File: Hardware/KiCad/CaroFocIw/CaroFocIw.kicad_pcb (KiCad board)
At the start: 4 copper layers, 174.5 x 99 mm, 130 parts, among them J1 Conn_01x04, J10 Conn_01x03, J11 Conn_01x03, J12 Conn_01x03, J13 Conn_01x03, J14 Conn_01x03, J15 Conn_01x06, J16 Conn_01x06, J17 Conn_01x06, J18 Conn_01x06, J19 Conn_01x02, J2 Conn_01x01, J20 Conn_01x02, J21 Conn_01x03, J22 Conn_01x03, J23 Conn_01x03, J24 Conn_01x03, J25 Conn_01x03, J26 Conn_01x03, J27 Conn_01x01, J28 Conn_01x01, J29 Conn_01x01, J3 Conn_01x01, J30 Conn_01x01, J4 Conn_01x01, J5 Conn_01x02, J6 Conn_01x01, J7 Conn_01x02, J8 Conn_01x02, J9 Conn_01x03, Q1 Q_NMOS_SGD, Q2 Q_NMOS_SGD, Q3 Q_NMOS_SGD, Q4 Q_NMOS_SGD, Q5 Q_NMOS_SGD, Q6 Q_NMOS_SGD, U1 TCAN332, U2 STM32F405RGTx, U3 TLE7185-1E, U4 ACS711xEXLT-15AB, U5 AS5048A, U6 ACS711xEXLT-15AB, U7 ACS711xEXLT-15AB, U8 LMR16006YQ3

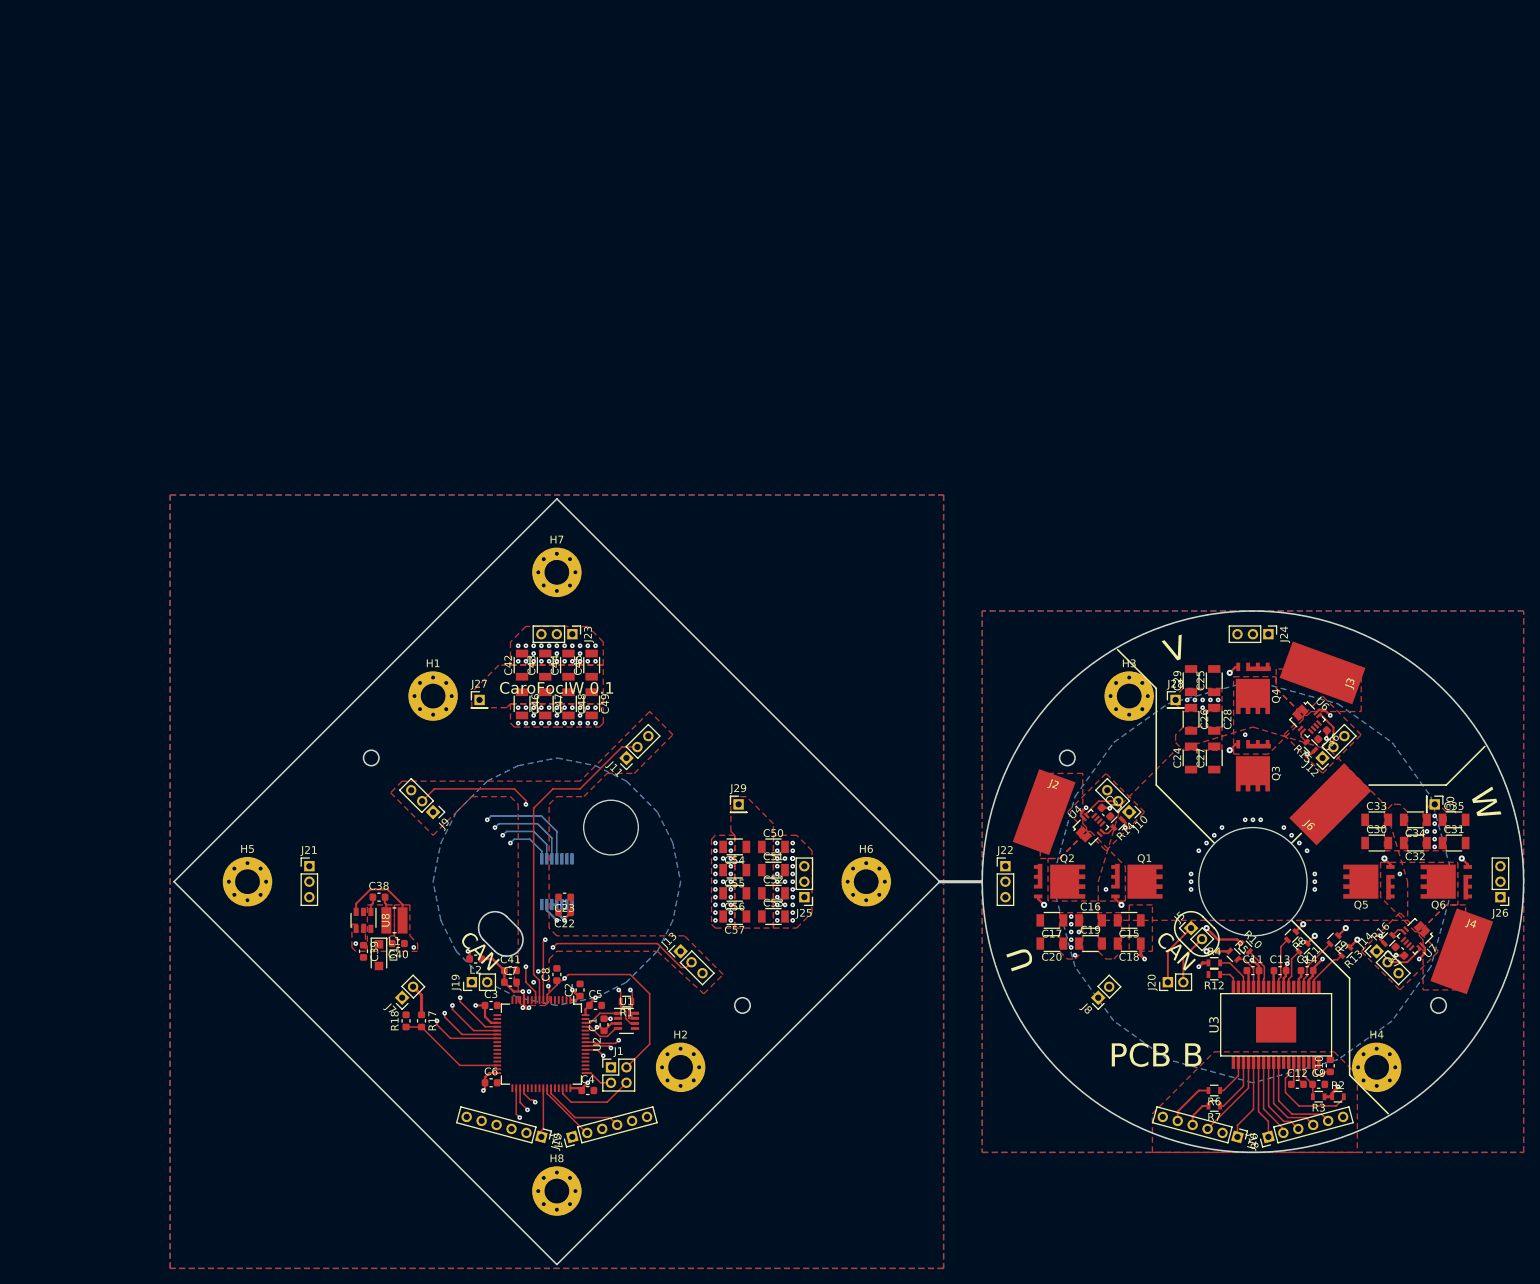
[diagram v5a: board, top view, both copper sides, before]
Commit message: Smaller form factor -> lots of rerouting needed. Moved gate driver to PCB A
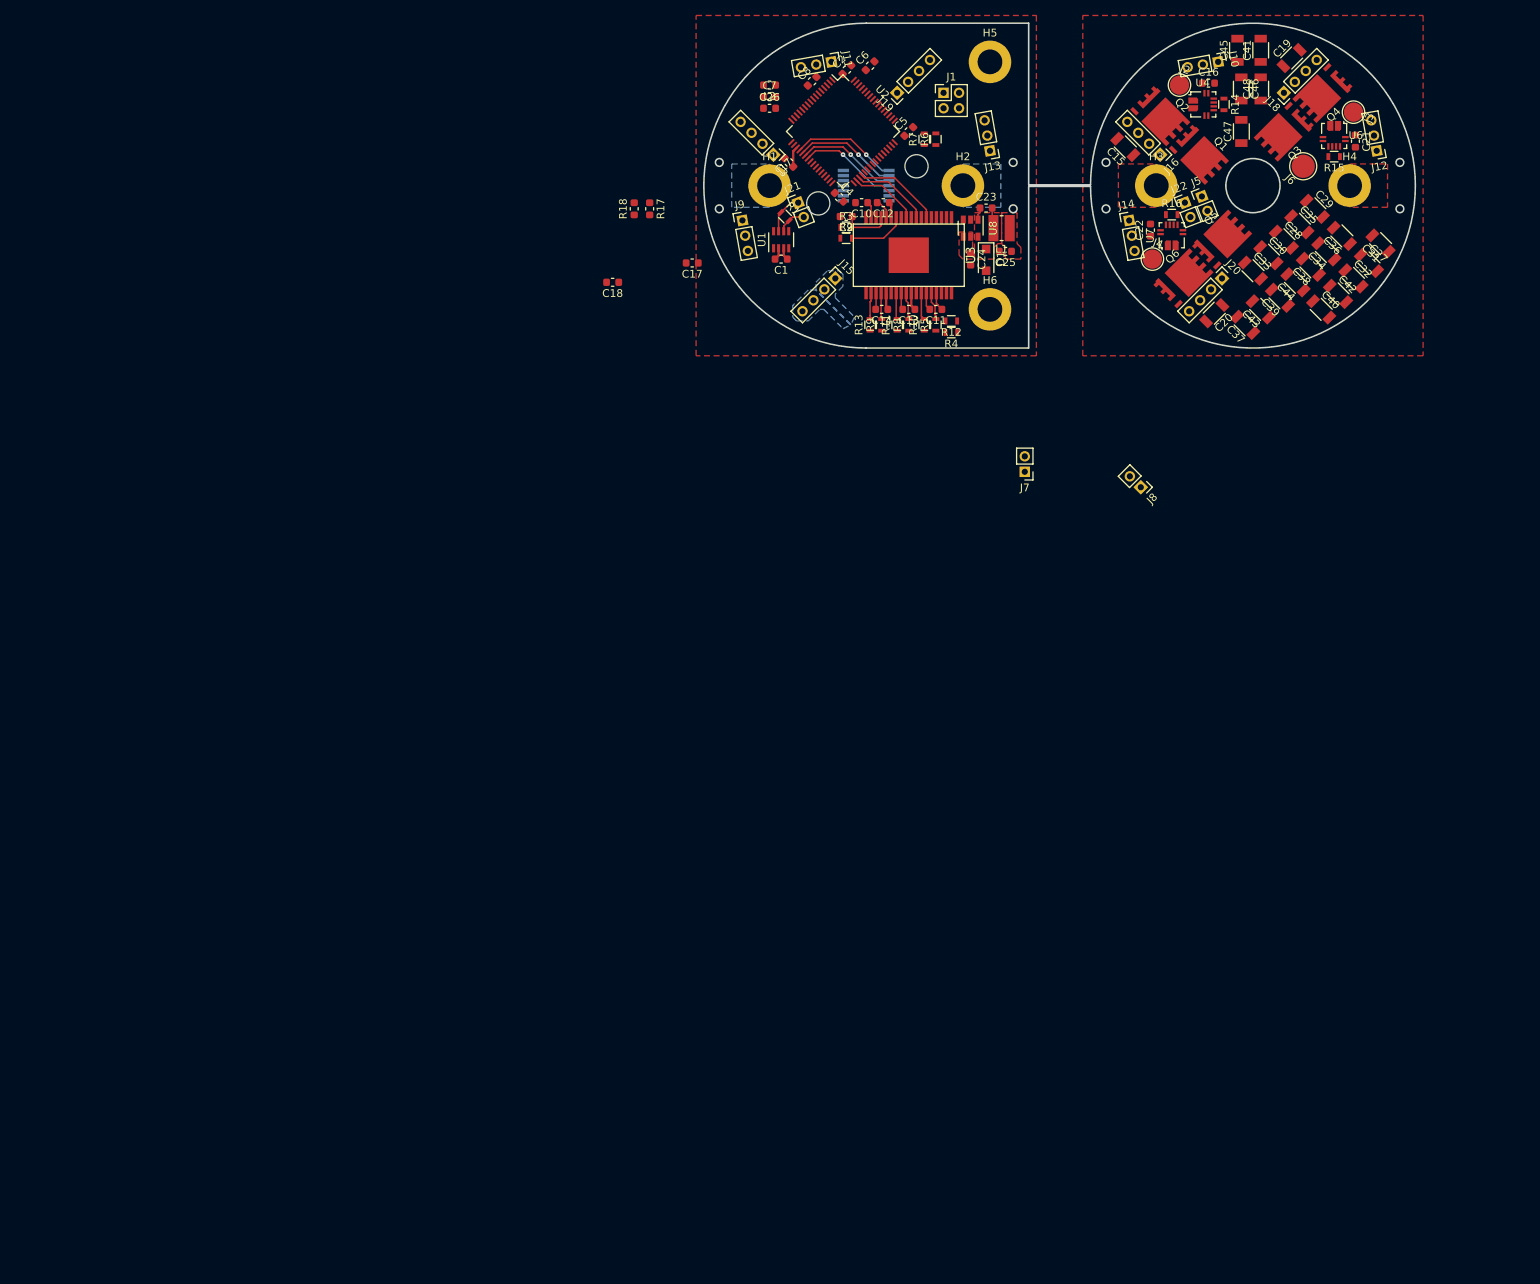
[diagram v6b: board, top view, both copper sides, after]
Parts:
- removed the C17 at (184.0, 130.0)
- removed the C18 at (194.0, 133.0)
- removed the C24 at (202.0, 109.0)
- removed the C25 at (205.0, 99.0)
- removed the C26 at (202.0, 104.0)
- removed C49, C50, C51, C52, C53, C54, C55, C56, C57: 22μ, 25V, Capacitors_SMD:C_1206
- removed H7, H8: MountingHole_Pad, MountingHole:MountingHole_3.2mm_M3_Pad_Via
- removed J23, J24, J25, J26: Conn_01x03, Connector_PinHeader_2.00mm:PinHeader_1x03_P2.00mm_Vertical
- removed J27, J28, J29, J30: Conn_01x01, Connector_PinHeader_2.00mm:PinHeader_1x01_P2.00mm_Vertical
- added C22: 100n, Capacitor_SMD:C_0603_1608Metric, F.Cu at (196.8, 40.8)
- added C38: C, Capacitors_SMD:C_1206, F.Cu at (217.5, 45.5)
- added C39: C, Capacitors_SMD:C_1206, F.Cu at (213.5, 49.5)
- added C40: C, Capacitors_SMD:C_1206, F.Cu at (218.8, 51.0)
- added C41: C, Capacitors_SMD:C_1206, F.Cu at (211.0, 17.5)
- C16: value 22μ, 25V -> 100n; footprint Capacitors_SMD:C_1206 -> Capacitor_SMD:C_0603_1608Metric
- C27, C28, C29, C30, C31, C32, C33, C34, C35, C42, C43, C44, C45, C46, C47, C48: value 22μ, 25V -> C
- C36, C37: value 100n -> C; footprint Capacitor_SMD:C_0603_1608Metric -> Capacitors_SMD:C_1206
- H1, H2, H3, H4, H5, H6: footprint MountingHole:MountingHole_3.2mm_M3_Pad_Via -> MountingHole:MountingHole_3.2mm_M3_ISO14580_Pad
- J15, J16, J17, J18: value Conn_01x06 -> Conn_01x04; footprint Connector_PinHeader_2.00mm:PinHeader_1x06_P2.00mm_Vertical -> Connector_PinHeader_2.00mm:PinHeader_1x04_P2.00mm_Vertical
- J19, J20: value Conn_01x02 -> Conn_01x04; footprint Connector_PinHeader_2.00mm:PinHeader_1x02_P2.00mm_Vertical -> Connector_PinHeader_2.00mm:PinHeader_1x04_P2.00mm_Vertical
- J2, J3, J4: footprint Wire_Pads:SolderWirePad_single_SMD_5x10mm -> TestPoint:TestPoint_Pad_D2.5mm
- J21, J22: value Conn_01x03 -> Conn_01x02; footprint Connector_PinHeader_2.00mm:PinHeader_1x03_P2.00mm_Vertical -> Connector_PinHeader_2.00mm:PinHeader_1x02_P2.00mm_Vertical
- J6: footprint Wire_Pads:SolderWirePad_single_SMD_5x10mm -> TestPoint:TestPoint_Pad_D3.0mm
- moved H5 143.0 mm to (176.0, 19.0)
- moved C6 140.3 mm to (160.5, 19.5), turned to 45 degrees
- moved J18 135.0 mm to (214.0, 23.0), turned to 135 degrees
- moved J1 133.1 mm to (170.0, 23.0)
- moved R7 130.5 mm to (167.5, 29.0), turned to 90 degrees
- moved J17 129.6 mm to (148.0, 31.0), turned to 225 degrees
- moved R6 128.2 mm to (169.0, 29.0), turned to 90 degrees
- moved R3 127.9 mm to (157.4, 40.4), turned to 0 degrees
- moved R2 127.9 mm to (157.4, 41.8)
- moved C9 127.8 mm to (157.4, 39.0), turned to 180 degrees
- moved J19 127.5 mm to (164.0, 23.0), turned to 135 degrees
- moved J16 127.4 mm to (198.0, 31.0), turned to 225 degrees
- moved C10 127.0 mm to (159.4, 37.2), turned to 180 degrees
- moved C12 126.0 mm to (162.2, 37.2), turned to 180 degrees
- moved U2 124.3 mm to (157.0, 28.0), turned to 315 degrees
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- renumbered C22 to C17, C23 to C18, C38 to C23, C39 to C24, C40 to C25, C41 to C26
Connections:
- C10 pad 2: GND_B -> GND
- C11 pad 2: /CurrentSensingU/PhaseIn -> /GateDriver/SourceUH
- C13 pad 2: /CurrentSensingV/PhaseIn -> /GateDriver/SourceVH
- C14 pad 2: /CurrentsensingW/PhaseIn -> /GateDriver/SourceWH
- C16 pad 1: +BATT -> 3.3VA_U
- C16 pad 2: GNDPWR -> AGND_U
- C21 pad 1: 3.3VA_U -> 3.3VA_V
- C21 pad 2: AGND_U -> AGND_V
- C36 pad 1: 3.3VA_V -> +BATT
- C36 pad 2: AGND_V -> GNDPWR
- C37 pad 1: 3.3VA_W -> +BATT
- C37 pad 2: AGND_W -> GNDPWR
- C42 pad 1: BattA1 -> +BATT
- C42 pad 2: GNDPWR_A -> GNDPWR
- C43 pad 1: BattA1 -> +BATT
- C43 pad 2: GNDPWR_A -> GNDPWR
- C44 pad 1: BattA1 -> +BATT
- C44 pad 2: GNDPWR_A -> GNDPWR
- C45 pad 1: BattA1 -> +BATT
- C45 pad 2: GNDPWR_A -> GNDPWR
- C46 pad 1: BattA1 -> +BATT
- C46 pad 2: GNDPWR_A -> GNDPWR
- C47 pad 1: BattA1 -> +BATT
- C47 pad 2: GNDPWR_A -> GNDPWR
- C48 pad 1: BattA1 -> +BATT
- C48 pad 2: GNDPWR_A -> GNDPWR
- C9 pad 2: GND_B -> GND
- J15 pad 1: /MCU/LogicUH -> /GateDriver/GateUH
- J15 pad 2: GND -> /GateDriver/SourceUH
- J15 pad 3: /MCU/GateDriverEnable -> /GateDriver/GateUL
- J15 pad 4: /MCU/~GateDriverErr1 -> /GateDriver/SourceUL
- J16 pad 1: /GateDriver/~LogicUH -> /HalfBridgeU/GateH
- J16 pad 2: GND_B -> /CurrentSensingU/PhaseIn
- J16 pad 3: /GateDriver/LogicGdEna -> /HalfBridgeU/GateL
- J16 pad 4: /GateDriver/~LogicGdErr1 -> GNDPWR
- J17 pad 1: /MCU/LogicUL -> /GateDriver/GateVH
- J17 pad 2: /MCU/LogicVH -> /GateDriver/SourceVH
- J17 pad 3: /MCU/LogicVL -> /GateDriver/GateVL
- J17 pad 4: /MCU/LogicWH -> /GateDriver/SourceVL
- J18 pad 1: /GateDriver/LogicUL -> /HalfBridgeV/GateH
- J18 pad 2: /GateDriver/~LogicVH -> /CurrentSensingV/PhaseIn
- J18 pad 3: /GateDriver/LogicVL -> /HalfBridgeV/GateL
- J18 pad 4: /GateDriver/~LogicWH -> GNDPWR
- J19 pad 1: /Can/CanH -> /GateDriver/GateWH
- J19 pad 2: /Can/CanL -> /GateDriver/SourceWH
- J20 pad 1: /PcbToPcbConnector/CanHB -> /HalfBridgeW/GateH
- J20 pad 2: /PcbToPcbConnector/CanLB -> /CurrentsensingW/PhaseIn
- J21 pad 1: GNDPWR_A -> /Can/CanH
- J21 pad 2: GNDPWR_A -> /Can/CanL
- J22 pad 1: GNDPWR -> /PcbToPcbConnector/CanHB
- J22 pad 2: GNDPWR -> /PcbToPcbConnector/CanLB
- R10 pad 1: /HalfBridgeU/GateL -> /GateDriver/GateUL
- R11 pad 1: /HalfBridgeV/GateL -> /GateDriver/GateVL
- R12 pad 2: GNDPWR -> GND
- R13 pad 1: /HalfBridgeW/GateL -> /GateDriver/GateWL
- R2 pad 1: +BATT -> BattA
- R3 pad 1: +BATT -> BattA
- R4 pad 1: +BATT -> BattA
- R5 pad 1: /HalfBridgeU/GateH -> /GateDriver/GateUH
- R6 pad 2: /GateDriver/~LogicGdErr2 -> /MCU/~GateDriverErr2
- R7 pad 2: /GateDriver/~LogicGdErr1 -> /MCU/~GateDriverErr1
- R8 pad 1: /HalfBridgeV/GateH -> /GateDriver/GateVH
- R9 pad 1: /HalfBridgeW/GateH -> /GateDriver/GateWH
- U2 pad 10: /MCU/CurrentW -> /MCU/CurrentU
- U2 pad 34: /MCU/LogicUL -> /GateDriver/LogicWL
- U2 pad 35: /MCU/LogicVL -> /GateDriver/LogicVL
- U2 pad 36: /MCU/LogicWL -> /GateDriver/LogicUL
- U2 pad 41: /MCU/LogicUH -> /MCU/LogicWH
- U2 pad 43: /MCU/LogicWH -> /MCU/LogicUH
- U2 pad 8: /MCU/CurrentU -> /MCU/CurrentW
- U3 pad 11: GND_B -> GND
- U3 pad 16: GND_B -> GND
- U3 pad 18: GND_B -> GND
- U3 pad 19: GNDPWR -> /GateDriver/SourceWL
- U3 pad 21: /CurrentsensingW/PhaseIn -> /GateDriver/SourceWH
- U3 pad 24: GNDPWR -> /GateDriver/SourceVL
- U3 pad 26: /CurrentSensingV/PhaseIn -> /GateDriver/SourceVH
- U3 pad 29: GNDPWR -> /GateDriver/SourceUL
- U3 pad 31: /CurrentSensingU/PhaseIn -> /GateDriver/SourceUH
- U3 pad 35: GNDPWR -> GND
- U3 pad 37: GNDPWR -> GND
- U3 pad 4: /GateDriver/LogicGdEna -> /MCU/GateDriverEnable
- U3 pad 5: /GateDriver/~LogicUH -> /MCU/LogicUH
- U3 pad 7: /GateDriver/~LogicVH -> /MCU/LogicVH
- U3 pad 9: /GateDriver/~LogicWH -> /MCU/LogicWH
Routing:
- net /HalfBridgeV/GateL: track 43.8 -> 0.00 mm, vias 2 -> 0
- net /MCU/CurrentV: track 41.8 -> 0.00 mm
- net /MCU/CurrentU: track 41.6 -> 0.00 mm, vias 2 -> 0
- net /Encoder/EncoderMosi: track 51.7 -> 12.8 mm, vias 2 -> 1
- net +3V3: track 38.2 -> 4.25 mm, vias 9 -> 0
- net /Encoder/EncoderMiso: track 46.4 -> 13.1 mm, vias 2 -> 1
- net /HalfBridgeU/GateL: track 32.3 -> 0.00 mm, vias 2 -> 0
- net /HalfBridgeV/GateH: track 31.0 -> 0.00 mm, vias 2 -> 0
- net /MCU/CurrentW: track 29.0 -> 0.00 mm, vias 2 -> 0
- net /Encoder/EncoderSclk: track 41.0 -> 13.5 mm, vias 2 -> 1
- net /MCU/~RST: track 27.1 -> 0.00 mm, vias 1 -> 0
- net /MCU/~GateDriverErr2: track 27.0 -> 0.00 mm, vias 1 -> 0
- net /Can/CanH: track 30.1 -> 5.31 mm, vias 1 -> 0
- net /MCU/~GateDriverErr1: track 23.4 -> 0.00 mm, vias 1 -> 0
- net /Can/CanL: track 25.8 -> 3.74 mm, vias 1 -> 0
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- added copper zone on B.Cu, net /GateDriver/SourceUH
- added copper zone on B.Cu, net /GateDriver/SourceUL
- removed copper zone on In2.Cu, net +3.3VA
- removed copper zone on In2.Cu, net +3V3
- removed copper zone on B.Cu, net +BATT
- removed copper zone on F.Cu, net +BATT
- removed copper zone on In2.Cu, net +BATT
- removed copper zone on F.Cu, net /CurrentSensingU/PhaseIn
- removed copper zone on In1.Cu, net /CurrentSensingU/PhaseIn
- removed copper zone on F.Cu, net /CurrentSensingU/PhaseOut
- removed copper zone on F.Cu, net /CurrentSensingV/PhaseIn
- removed copper zone on In1.Cu, net /CurrentSensingV/PhaseIn
- removed copper zone on F.Cu, net /CurrentSensingV/PhaseOut
- removed copper zone on F.Cu, net /CurrentsensingW/PhaseIn
- removed copper zone on In1.Cu, net /CurrentsensingW/PhaseIn
- removed copper zone on F.Cu, net /CurrentsensingW/PhaseOut
- removed copper zone on In2.Cu, net 3.3VA_U
- removed copper zone on In2.Cu, net 3.3VA_W
- removed copper zone on F.Cu, net AGND_U
- removed copper zone on In1.Cu, net AGND_U
- removed copper zone on F.Cu, net AGND_V
- removed copper zone on F.Cu, net AGND_W
- removed copper zone on In1.Cu, net AGND_W
- removed copper zone on F.Cu, net BattA1
- removed copper zone on F.Cu, net BattA2
- removed copper zone on B.Cu, net GND
- removed copper zone on In1.Cu, net GND
- removed copper zone on F.Cu, net GNDA
- removed copper zone on In1.Cu, net GNDA
- removed copper zone on B.Cu, net GNDPWR
- removed copper zone on In1.Cu, net GNDPWR
- removed copper zone on In2.Cu, net GNDPWR
- removed copper zone on F.Cu, net GNDPWR_A
- removed copper zone on F.Cu, net GND_B
- removed copper zone on In1.Cu, net GND_B
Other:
- board size 174.5 x 99 mm -> 92 x 42 mm
- board text removed: "CAN"
- board text removed: "CaroFocIW 0.1"
- board text removed: "PCB B"
- board text removed: "U"
- board text removed: "V"
- board text removed: "W"

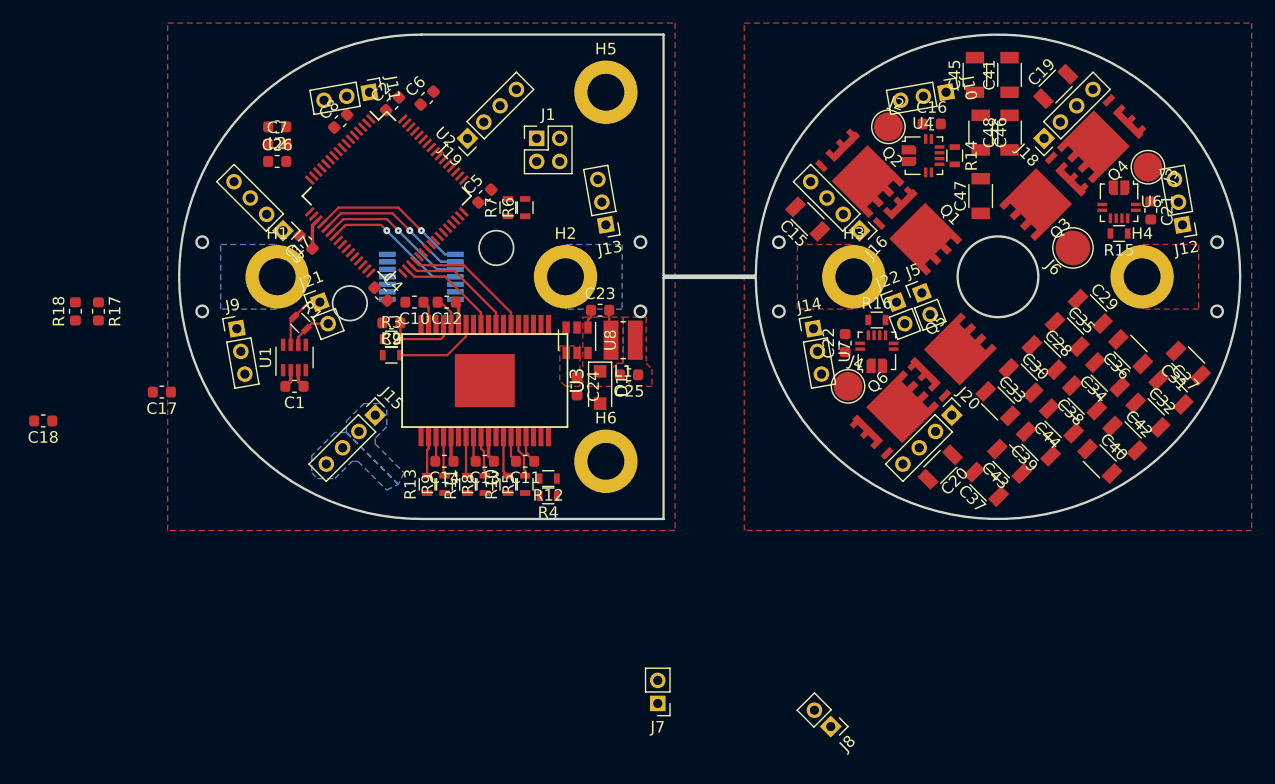
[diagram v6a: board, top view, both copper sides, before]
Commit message: Some more routing, PCB B almost finished
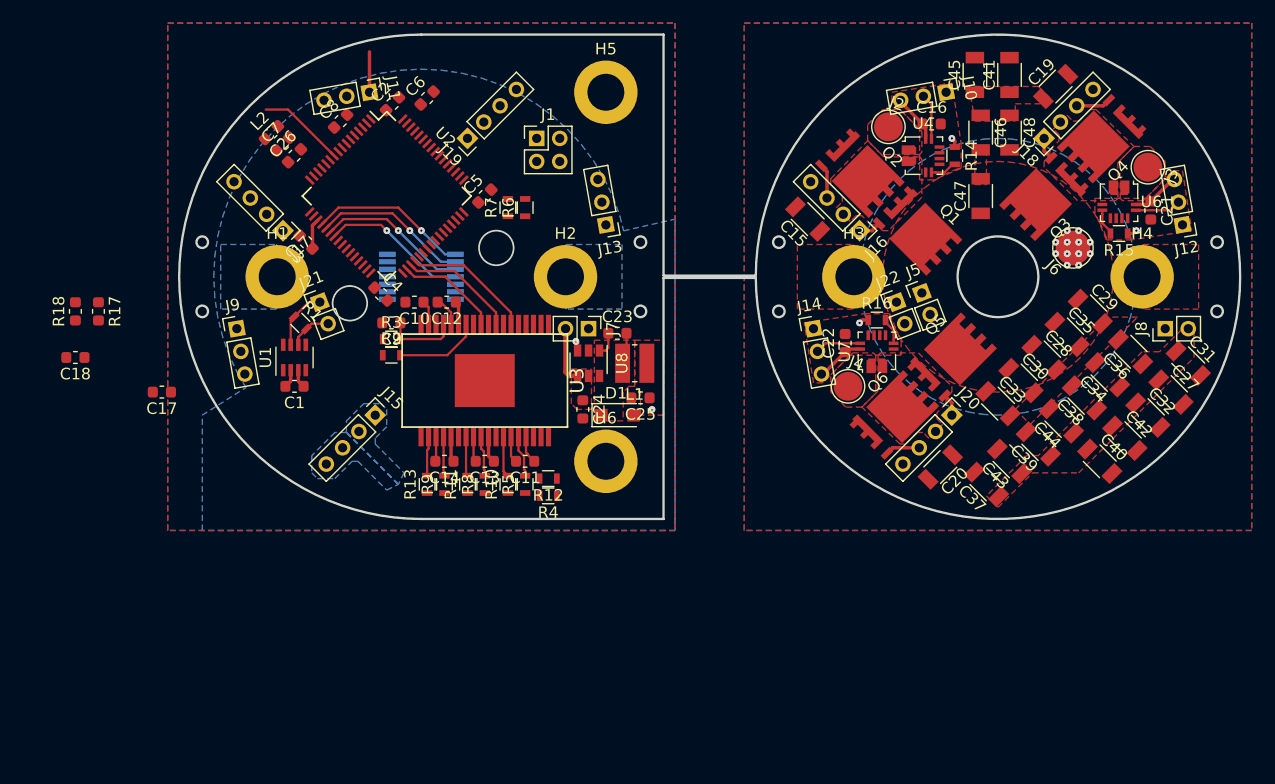
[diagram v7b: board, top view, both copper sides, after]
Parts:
- moved J8 45.1 mm to (224.5, 39.5), turned to 90 degrees
- moved J7 33.0 mm to (174.5, 39.5), turned to 270 degrees
- moved C18 6.17 mm to (130.0, 42.0)
- moved D1 2.83 mm to (177.0, 47.0), turned to 0 degrees
- moved C23 2.50 mm to (177.0, 39.9)
- moved C25 2.24 mm to (179.0, 45.5)
- moved L1 2.24 mm to (178.5, 42.5)
- moved U8 2.24 mm to (174.5, 42.5)
- moved C24 2.06 mm to (174.0, 46.5)
- moved C26 1.58 mm to (149.0, 24.5), turned to 45 degrees
- moved L2 0.71 mm to (147.0, 22.5), turned to 45 degrees
- moved C7 0.50 mm to (148.0, 23.5), turned to 45 degrees
- turned C31 to 315 degrees
- turned C48 to 270 degrees
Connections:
- H5 pad 1: GNDPWR_A -> Net-(H5-Pad1)
- H6 pad 1: GNDPWR_A -> Net-(H6-Pad1)
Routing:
- net /MCU/CurrentU: track 0.00 -> 7.60 mm
- net /GateDriver/GateUH: track 7.24 -> 0.00 mm
- net /GateDriver/GateUL: track 5.14 -> 0.00 mm
- net 3.3VA_V: track 0.00 -> 5.11 mm, vias 0 -> 1
- net 3.3VA_W: track 0.00 -> 5.11 mm, vias 0 -> 1
- net 3.3VA_U: track 0.00 -> 5.11 mm, vias 0 -> 1
- net BattA: track 0.00 -> 4.96 mm
- net /CurrentsensingW/AnalogOut: track 0.00 -> 3.99 mm
- net /CurrentSensingV/AnalogOut: track 0.00 -> 3.99 mm
- net /CurrentSensingU/AnalogOut: track 0.00 -> 3.99 mm
- net GNDA: track 0.00 -> 3.50 mm
- net /HalfBridgeW/GateL: track 0.00 -> 2.99 mm
- net /HalfBridgeV/GateL: track 0.00 -> 2.99 mm
- net /HalfBridgeU/GateL: track 0.00 -> 2.99 mm
- net Net-(R14-Pad2): track 0.00 -> 2.31 mm
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- added copper zone on In1.Cu, net +3.3VA
- added copper zone on In2.Cu, net +3V3
- added copper zone on B.Cu, net +BATT
- added copper zone on F.Cu, net +BATT
- added copper zone on In1.Cu, net +BATT
- added copper zone on F.Cu, net /CurrentSensingU/PhaseIn
- added copper zone on F.Cu, net /CurrentSensingU/PhaseOut
- added copper zone on F.Cu, net /CurrentSensingV/PhaseIn
- added copper zone on F.Cu, net /CurrentSensingV/PhaseOut
- added copper zone on F.Cu, net /CurrentsensingW/PhaseIn
- added copper zone on F.Cu, net /CurrentsensingW/PhaseOut
- added copper zone on In2.Cu, net 3.3VA_U
- added copper zone on In2.Cu, net 3.3VA_W
- added copper zone on F.Cu, net AGND_U
- added copper zone on In1.Cu, net AGND_U
- added copper zone on F.Cu, net AGND_V
- added copper zone on F.Cu, net AGND_W
- added copper zone on In1.Cu, net AGND_W
- added copper zone on B.Cu, net GND
- added copper zone on In1.Cu, net GND
- added copper zone on B.Cu, net GNDA
- added copper zone on In2.Cu, net GNDA
- added copper zone on B.Cu, net GNDPWR
- added copper zone on In2.Cu, net GNDPWR

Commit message: more layout
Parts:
- moved R18 25.7 mm to (155.0, 44.0)
- moved R17 21.8 mm to (153.0, 44.0)
- moved C18 19.6 mm to (149.0, 47.0)
- moved C17 12.2 mm to (149.0, 49.0)
- moved C26 2.24 mm to (148.0, 22.5)
- moved C7 2.24 mm to (150.0, 24.5)
- moved L2 2.24 mm to (148.0, 24.5), turned to 225 degrees
- moved R6 0.50 mm to (169.5, 29.0)
- moved R7 0.50 mm to (168.0, 29.0)
- moved C5 0.41 mm to (165.4, 28.4)
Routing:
- net /Can/CanTx: track 0.00 -> 33.5 mm, vias 0 -> 2
- net /Can/CanRx: track 0.00 -> 29.5 mm, vias 0 -> 2
- net /MCU/GateDriverEnable: track 0.00 -> 19.6 mm
- net +3V3: track 5.12 -> 21.7 mm, vias 2 -> 7
- net /MCU/LogicUH: track 0.00 -> 11.2 mm
- net /MCU/LogicVH: track 0.00 -> 10.9 mm, vias 0 -> 2
- net /MCU/~GateDriverErr2: track 0.00 -> 10.8 mm
- net Net-(R7-Pad1): track 0.00 -> 10.1 mm
- net /MCU/LogicWH: track 0.00 -> 10.0 mm, vias 0 -> 2
- net Net-(R6-Pad1): track 0.00 -> 9.79 mm
- net /MCU/~GateDriverErr1: track 0.00 -> 9.11 mm
- net /MCU/SWCLK: track 0.00 -> 6.75 mm, vias 0 -> 1
- net Net-(R4-Pad2): track 0.00 -> 5.77 mm
- net /MCU/CurrentW: track 0.00 -> 5.16 mm
- net /MCU/CurrentV: track 0.00 -> 5.16 mm
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- added copper zone on F.Cu, net +3.3VA
- added copper zone on B.Cu, net +3V3
- added copper zone on F.Cu, net 3.3VA_W
- removed copper zone on B.Cu, net /GateDriver/SourceUH
- removed copper zone on B.Cu, net /GateDriver/SourceUL
